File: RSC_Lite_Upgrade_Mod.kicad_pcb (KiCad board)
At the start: 2 copper layers, 36.8 x 48 mm, 30 parts, among them J1 USB_B_Micro, J2 Boot Mode, J3 SWD, J4 JTAG, SW1 RESET, U1 STM32F103C8Tx, Y1 8Mhz

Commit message: Add gerbers and firmware for revision 1
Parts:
- added R9: 1.5K, Resistor_SMD:R_1206_3216Metric_Pad1.30x1.75mm_HandSolder, F.Cu at (214.1, 54.4)
- C1: value 1uF -> 100nF
- R6: value 10K -> 1K
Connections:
- RN1 pad 1: GND -> VCC
- RN1 pad 2: GND -> VCC
- RN1 pad 3: GND -> VCC
- RN1 pad 4: GND -> VCC
- RN2 pad 1: GND -> VCC
- RN2 pad 2: GND -> VCC
- RN2 pad 3: GND -> VCC
- RN2 pad 4: GND -> VCC
- U1 pad 29: unconnected-(U1-PA8-Pad29) -> /USB_PULL
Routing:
- net VCC: track 152.1 -> 181.6 mm, vias 8 -> 10
- net /USB_PULL: track 0.00 -> 20.2 mm, vias 0 -> 2
- net /USB_D+: track 24.3 -> 29.4 mm, vias 2 -> 4
- net GND: track 348.9 -> 346.9 mm, vias 26 -> 27
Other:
- board text added: "Rev.1"
- board text removed: "Rev.0"

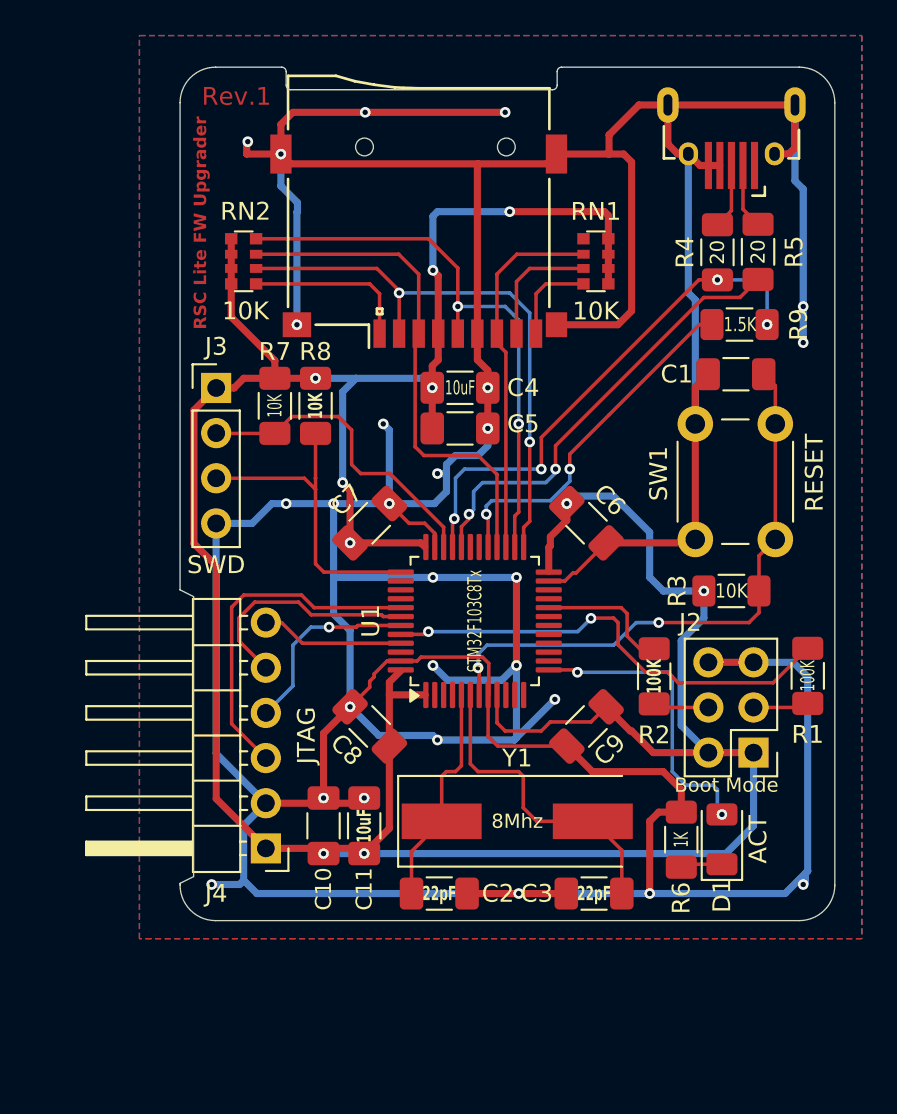
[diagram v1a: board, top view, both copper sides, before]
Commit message: Begin removing unnecessary components
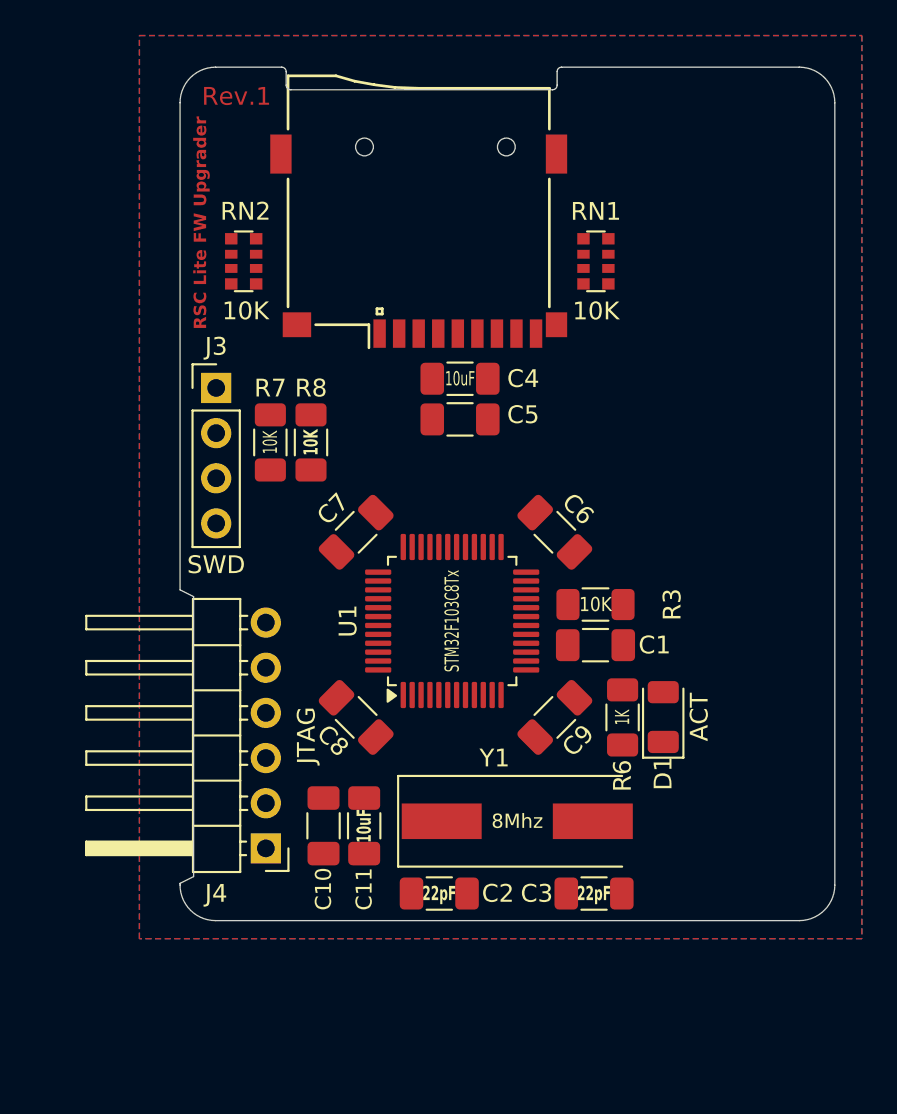
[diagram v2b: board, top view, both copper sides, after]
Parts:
- removed J1: USB_B_Micro, mod:Conn_USBmicro-B_ebay-side_TH
- removed J2: Boot Mode, Connector_PinHeader_2.54mm:PinHeader_2x03_P2.54mm_Vertical
- removed R1, R2: 100K, Resistor_SMD:R_1206_3216Metric_Pad1.30x1.75mm_HandSolder
- removed R4, R5: 20, Resistor_SMD:R_1206_3216Metric_Pad1.30x1.75mm_HandSolder
- removed R9: 1.5K, Resistor_SMD:R_1206_3216Metric_Pad1.30x1.75mm_HandSolder
- removed SW1: RESET, Button_Switch_THT:SW_PUSH_6mm
- moved C1 17.2 mm to (206.0, 72.4), turned to 0 degrees
- moved R3 7.68 mm to (206.0, 70.1), turned to 0 degrees
- moved D1 7.63 mm to (209.8, 76.4)
- moved R6 7.63 mm to (207.5, 76.5)
- moved R7 2.07 mm to (187.7, 61.0)
- moved R8 2.07 mm to (190.0, 61.0)
- moved C6 1.85 mm to (203.7, 66.0)
- moved C9 1.85 mm to (203.7, 76.5)
- moved U1 1.27 mm to (197.9, 71.0)
- moved C7 0.92 mm to (192.5, 66.0)
- moved C8 0.92 mm to (192.5, 76.5)
- moved C5 0.51 mm to (198.4, 59.7)
- moved C4 0.51 mm to (198.4, 57.4)
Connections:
- U1 pad 29: /USB_PULL -> unconnected-(U1-PA8-Pad29)
- U1 pad 44: /BOOT0 -> GND
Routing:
- net GND: track 346.9 -> 0.00 mm, vias 27 -> 0
- net VCC: track 181.6 -> 0.00 mm, vias 10 -> 0
- net /~{RESET}: track 33.2 -> 0.00 mm, vias 2 -> 0
- net /SPI2_SCK: track 32.3 -> 0.00 mm, vias 2 -> 0
- net /SPI2_SD_CS: track 32.1 -> 0.00 mm, vias 2 -> 0
- net /USB_D+: track 29.4 -> 0.00 mm, vias 4 -> 0
- net /SPI2_MOSI: track 28.7 -> 0.00 mm
- net /BOOT0: track 26.3 -> 0.00 mm, vias 2 -> 0
- net /USB_D-: track 25.2 -> 0.00 mm, vias 2 -> 0
- net /SPI2_MISO: track 20.9 -> 0.00 mm
- net /USB_PULL: track 20.2 -> 0.00 mm, vias 2 -> 0
- net /JTAG_TDO: track 19.4 -> 0.00 mm
- net /SWCLK: track 18.2 -> 0.00 mm
- net /SWDIO: track 18.0 -> 0.00 mm
- net Net-(U1-PD1): track 17.9 -> 0.00 mm
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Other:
- board text removed: "BOOT0"
- board text removed: "BOOT1"

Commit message: Rerouted the board
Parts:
- removed the C10 at (190.7, 82.5)
- C1, C2, C3, C4, C5, C6, C7, C8, C9: footprint Capacitor_SMD:C_1206_3216Metric_Pad1.33x1.80mm_HandSolder -> Capacitor_SMD:C_0805_2012Metric_Pad1.18x1.45mm_HandSolder
- C10: renamed from C11; footprint Capacitor_SMD:C_1206_3216Metric_Pad1.33x1.80mm_HandSolder -> Capacitor_SMD:C_0805_2012Metric_Pad1.18x1.45mm_HandSolder
- D1: footprint LED_SMD:LED_1206_3216Metric -> LED_SMD:LED_0805_2012Metric_Pad1.15x1.40mm_HandSolder
- R3, R6, R7, R8: footprint Resistor_SMD:R_1206_3216Metric_Pad1.30x1.75mm_HandSolder -> Resistor_SMD:R_0805_2012Metric_Pad1.20x1.40mm_HandSolder
- moved C3 12.0 mm to (196.6, 78.7)
- moved C2 9.22 mm to (192.0, 78.7)
- moved D1 6.63 mm to (203.2, 77.0)
- moved Y1 6.27 mm to (195.3, 82.5)
- moved R6 6.12 mm to (203.2, 80.8), turned to -90 degrees
- moved C10 5.67 mm to (187.5, 83.8)
- moved RN1 3.88 mm to (202.9, 53.1)
- moved C1 3.81 mm to (202.2, 72.4)
- moved C6 3.81 mm to (199.9, 66.0)
- moved C7 3.81 mm to (188.7, 66.0)
- moved C8 3.81 mm to (188.7, 76.5)
- moved C9 3.81 mm to (199.9, 76.5)
- moved R3 3.81 mm to (202.2, 70.1)
- moved U1 3.81 mm to (194.1, 71.0)
- moved XS1 3.39 mm to (193.5, 46.7)
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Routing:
- net GND: track 0.00 -> 237.2 mm, vias 0 -> 26
- net VCC: track 0.00 -> 172.3 mm, vias 0 -> 6
- net /SPI2_SCK: track 0.00 -> 31.4 mm, vias 0 -> 3
- net /SPI2_MOSI: track 0.00 -> 27.8 mm, vias 0 -> 2
- net /SPI2_MISO: track 0.00 -> 24.9 mm
- net /SPI2_SD_CS: track 0.00 -> 23.9 mm
- net /JTAG_TDO: track 0.00 -> 15.6 mm, vias 0 -> 1
- net /SWCLK: track 0.00 -> 13.4 mm
- net /SWDIO: track 0.00 -> 13.4 mm
- net Net-(U1-PD1): track 0.00 -> 11.6 mm
- net /~{RESET}: track 0.00 -> 11.4 mm, vias 0 -> 2
- net /JTAG_TCK: track 0.00 -> 9.87 mm, vias 0 -> 1
- net Net-(U1-PD0): track 0.00 -> 9.13 mm
- net Net-(RN2-R4.2): track 0.00 -> 9.03 mm
- net /JTAG_TDI: track 0.00 -> 7.91 mm, vias 0 -> 1
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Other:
- board size 36.8 x 48 mm -> 21.8 x 42.4 mm
- board text removed: "RSC Lite FW Upgrader"
- board text removed: "Rev.1"

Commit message: Route again
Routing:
- net GND: track 237.2 -> 242.0 mm, vias 26 -> 28
- net VCC: track 172.3 -> 172.9 mm
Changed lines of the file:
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@@
 		)
 		(property "Value" "JTAG"
-			(at -2.54 10.414 90)
+			(at -1.778 10.414 90)
 			(layer "F.SilkS")
 			(effects
@@
 		)
 		(property "Value" "SWD"
-			(at 2.54 9.144 90)
+			(at 0.254 9.906 180)
 			(layer "F.SilkS")
 			(effects
@@
 	)
 	(gr_text "GND"
-		(at 185.928 65.532 0)
+		(at 185.928 67.31 0)
 		(layer "B.SilkS")
 		(effects
@@
 	)
 	(gr_text "TDO"
-		(at 188.722 78.74 0)
+		(at 185.674 78.74 0)
 		(layer "B.SilkS")
 		(effects
@@
 	)
 	(gr_text "SWDIO"
-		(at 185.674 64.278 0)
+		(at 185.674 62.23 0)
 		(layer "B.SilkS")
 		(effects
@@
 	)
 	(gr_text "VCC"
-		(at 185.674 61.738 0)
+		(at 185.674 59.69 0)
 		(layer "B.SilkS")
 		(effects
@@
 	)
 	(gr_text "TMS"
-		(at 188.722 71.12 0)
+		(at 185.674 71.12 0)
 		(layer "B.SilkS")
 		(effects
@@
 	)
 	(gr_text "TDI"
-		(at 188.722 73.66 0)
+		(at 185.674 73.66 0)
 		(layer "B.SilkS")
 		(effects
@@
 	)
 	(gr_text "TCK"
-		(at 188.722 76.2 0)
+		(at 185.674 76.2 0)
 		(layer "B.SilkS")
 		(effects
@@
 	)
 	(gr_text "VCC"
-		(at 188.722 83.82 0)
+		(at 185.674 83.82 0)
 		(layer "B.SilkS")
 		(effects
@@
 	)
 	(gr_text "GND"
-		(at 188.722 81.28 0)
+		(at 185.674 81.28 0)
 		(layer "B.SilkS")
 		(effects
@@
 	)
 	(segment
+		(start 186.182 74.676)
+		(end 186.944 74.676)
+		(width 0.2)
+		(layer "F.Cu")
+		(net 2)
+	)
+	(segment
 		(start 190.997646 72.644)
 		(end 190.997646 72.048736)
@@
 	)
 	(segment
+		(start 186.944 74.676)
+		(end 187.988377 75.720377)
+		(width 0.2)
+		(layer "F.Cu")
+		(net 2)
+	)
+	(segment
 		(start 187.988377 74.139623)
 		(end 188.846854 73.281146)
@@
 	)
 	(segment
+		(start 185.928 68.58)
+		(end 184.658 67.31)
+		(width 0.2)
+		(layer "F.Cu")
+		(net 2)
+	)
+	(segment
 		(start 199.136 78.232)
 		(end 199.898 78.994)
@@
 	)
 	(segment
+		(start 185.928 69.342)
+		(end 185.928 68.58)
+		(width 0.2)
+		(layer "F.Cu")
+		(net 2)
+	)
+	(segment
 		(start 194.564 72.644)
 		(end 191.77 72.644)
@@
 	)
 	(via
+		(at 185.928 69.342)
+		(size 0.6)
+		(drill 0.3)
+		(layers "F.Cu" "B.Cu")
+		(free yes)
+		(net 2)
+	)
+	(via
 		(at 194.31 78.74)
 		(size 0.6)
@@
 	)
 	(via
+		(at 186.182 74.676)
+		(size 0.6)
+		(drill 0.3)
+		(layers "F.Cu" "B.Cu")
+		(free yes)
+		(net 2)
+	)
+	(via
 		(at 194.31 71.374)
 		(size 0.6)
@@
 	)
 	(segment
-		(start 200.631623 75.720377)
-		(end 200.631623 84.102377)
+		(start 183.408 69.576)
+		(end 184.144884 68.839116)
 		(width 0.4)
 		(layer "B.Cu")
@@
 	)
 	(segment
-		(start 186.182 65.786)
-		(end 186.182 67.828233)
+		(start 184.658 83.82)
+		(end 183.408 82.57)
+		(width 0.4)
+		(layer "B.Cu")
+		(net 5)
+	)
+	(segment
+		(start 200.631623 75.720377)
+		(end 200.631623 84.102377)
 		(width 0.4)
 		(layer "B.Cu")
@@
 	)
 	(segment
-		(start 183.408 70.602233)
-		(end 183.408 82.57)
+		(start 185.171116 68.839116)
+		(end 186.182 67.828233)
 		(width 0.4)
 		(layer "B.Cu")
@@
 	(segment
 		(start 183.408 82.57)
-		(end 184.658 83.82)
+		(end 183.408 69.576)
 		(width 0.4)
 		(layer "B.Cu")
@@
 	(segment
 		(start 186.182 67.828233)
-		(end 183.408 70.602233)
+		(end 186.182 65.786)
 		(width 0.4)
 		(layer "B.Cu")
@@
 		(width 0.4)
 		(layer "B.Cu")
+		(net 5)
+	)
+	(segment
+		(start 184.144884 68.839116)
+		(end 185.171116 68.839116)
+		(width 0.4)
+		(layer "B.Cu")

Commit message: Some more rerouting
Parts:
- U1: value STM32F103C8Tx -> 32F103C8T6
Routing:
- net GND: track 242.0 -> 247.7 mm, vias 28 -> 30
- net /SPI2_MISO: track 24.9 -> 19.6 mm
- net /SPI2_MOSI: track 27.8 -> 23.6 mm, vias 2 -> 0
- net /SPI2_SD_CS: track 23.9 -> 28.0 mm, vias 0 -> 2
- net VCC: track 172.9 -> 174.7 mm
- net /SPI2_SCK: track 31.4 -> 32.2 mm

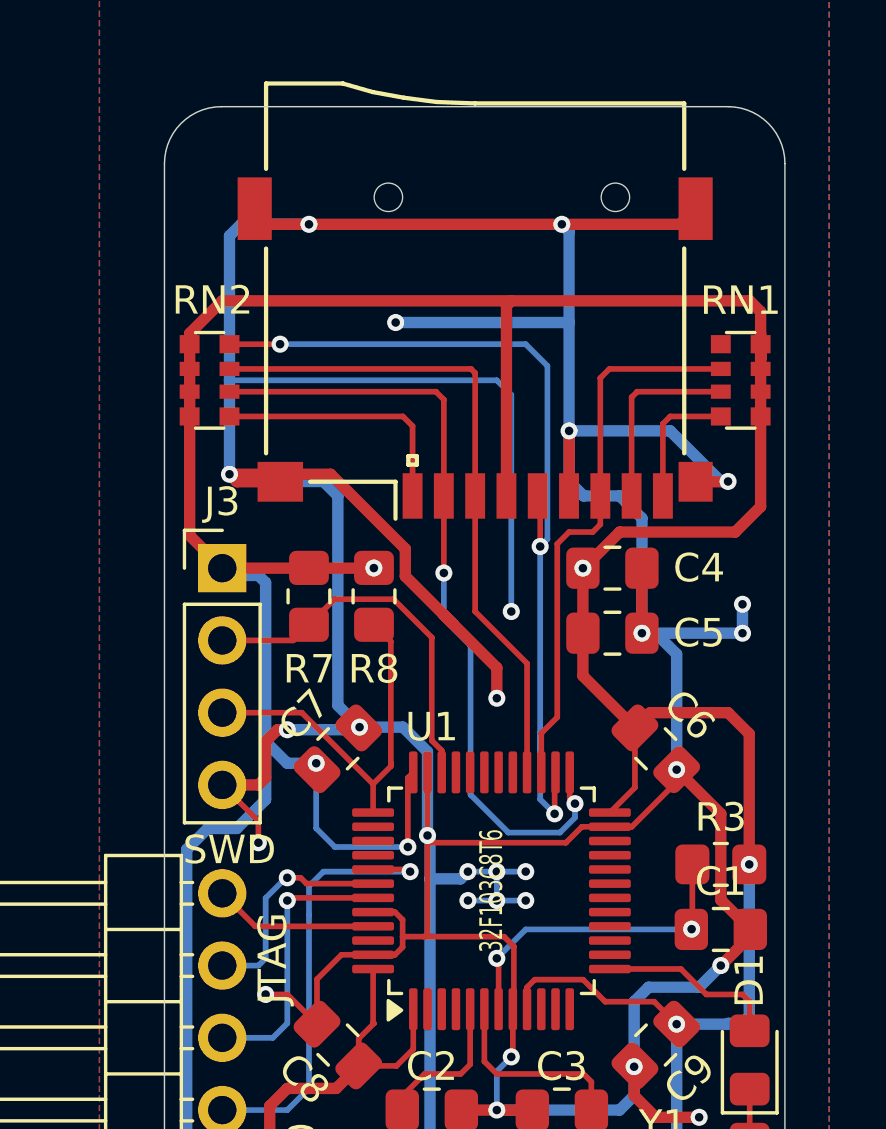
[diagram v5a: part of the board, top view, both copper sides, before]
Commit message: Update some routing and silkscreen
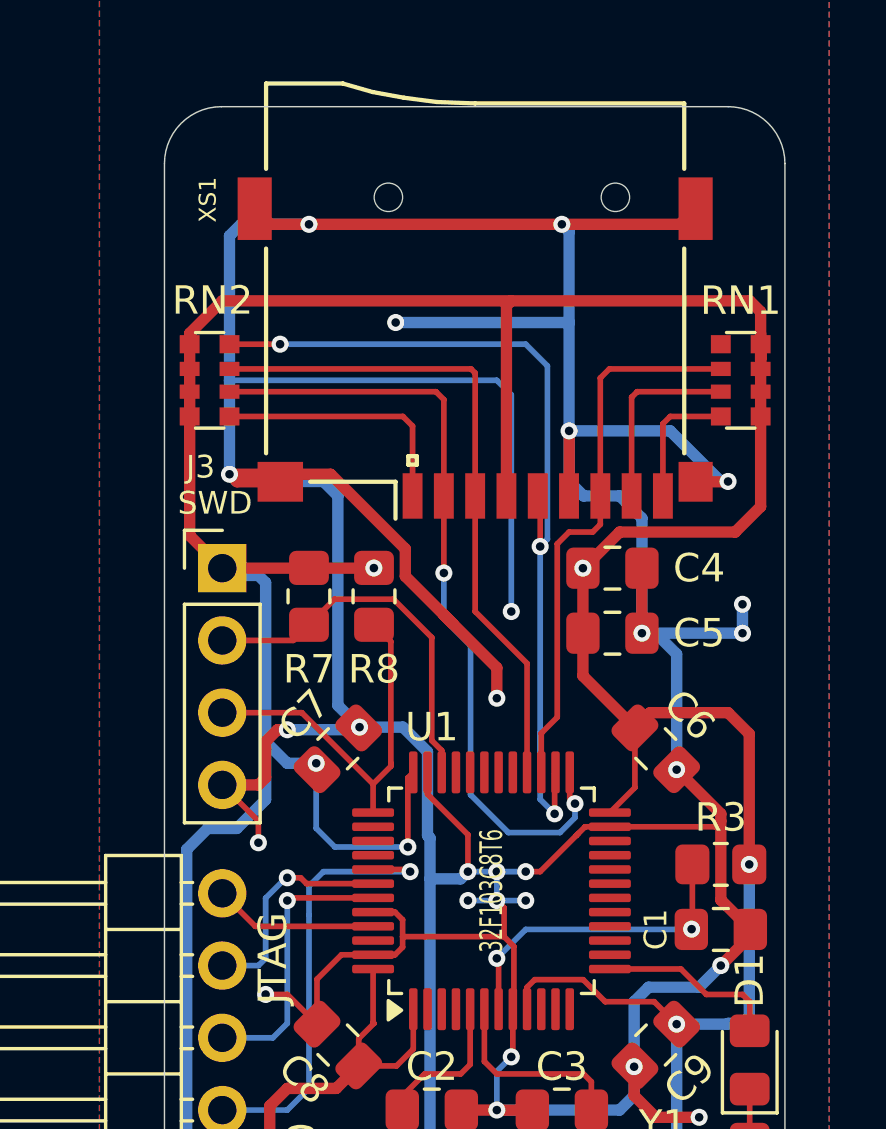
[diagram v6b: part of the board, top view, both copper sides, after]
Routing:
- net GND: track 247.7 -> 245.4 mm, vias 30 -> 29
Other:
- board text added: "Lava RSC Lite Upgrade board"
- board text added: "Rev.2"
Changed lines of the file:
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@@
 		(at 193.548 46.652 180)
 		(property "Reference" "XS1"
-			(at 0 1 0)
-			(layer "F.Fab")
+			(at 9.398 -0.084 90)
+			(layer "F.SilkS")
 			(effects
 				(font
@@
 		(tags "Through hole pin header THT 1x04 2.54mm single row")
 		(property "Reference" "J3"
-			(at 0 -2.33 0)
+			(at -0.762 -3.556 0)
 			(layer "F.SilkS")
 			(effects
 				(font
-					(size 1 1)
+					(size 0.8 0.8)
 					(thickness 0.15)
 				)
@@
 		)
 		(property "Value" "SWD"
-			(at 0.254 9.906 180)
+			(at -0.254 -2.286 180)
 			(layer "F.SilkS")
 			(effects
 				(font
-					(size 1 1)
+					(size 0.8 0.8)
 					(thickness 0.15)
 				)
@@
 		(tags "capacitor handsolder")
 		(property "Reference" "C1"
-			(at 0 -1.68 0)
+			(at -2.286 0 90)
 			(layer "F.SilkS")
 			(effects
 				(font
-					(size 1 1)
+					(size 0.8 0.8)
 					(thickness 0.15)
 				)
@@
 		)
 	)
+	(gr_text "Lava RSC Lite Upgrade board"
+		(at 201.93 60.706 90)
+		(layer "B.SilkS")
+		(effects
+			(font
+				(size 2 1.4)
+				(thickness 0.3)
+				(bold yes)
+			)
+			(justify mirror)
+		)
+	)
 	(gr_text "SWDIO"
 		(at 185.674 62.23 0)
@@
 		)
 	)
+	(gr_text "Rev.2"
+		(at 202.438 82.804 90)
+		(layer "B.SilkS")
+		(effects
+			(font
+				(size 1 0.7)
+				(thickness 0.15)
+				(bold yes)
+			)
+			(justify mirror)
+		)
+	)
 	(gr_text "TMS"
 		(at 185.674 71.12 0)
@@
 	)
 	(segment
-		(start 199.055056 68.781146)
-		(end 200.631623 67.204579)
-		(width 0.2)
-		(layer "F.Cu")
-		(net 2)
-	)
-	(segment
 		(start 186.182 74.676)
 		(end 186.944 74.676)
@@
 	)
 	(segment
-		(start 202.428 56.652)
-		(end 202.438 56.642)
-		(width 0.4)
+		(start 198.285146 68.781146)
+		(end 201.982854 68.781146)
+		(width 0.2)
 		(layer "F.Cu")
 		(net 2)
 	)
 	(segment
-		(start 194.31 63.191106)
-		(end 194.31 64.262)
+		(start 202.428 56.652)
+		(end 202.438 56.642)
 		(width 0.4)
 		(layer "F.Cu")
@@
 	)
 	(segment
-		(start 202.184 71.3525)
-		(end 202.184 68.326)
+		(start 194.31 63.191106)
+		(end 194.31 64.262)
 		(width 0.4)
 		(layer "F.Cu")
@@
 	)
 	(segment
+		(start 194.564 71.628)
+		(end 194.31 71.374)
+		(width 0.2)
+		(layer "F.Cu")
+		(net 2)
+	)
+	(segment
 		(start 186.944 74.676)
 		(end 187.988377 75.720377)
@@
 	)
 	(segment
+		(start 197.104 69.088)
+		(end 195.834 70.358)
+		(width 0.2)
+		(layer "F.Cu")
+		(net 2)
+	)
+	(segment
 		(start 186.182 65.786)
 		(end 186.598 65.37)
@@
 	)
 	(segment
+		(start 191.872646 67.638556)
+		(end 193.294 69.05991)
+		(width 0.2)
+		(layer "F.Cu")
+		(net 2)
+	)
+	(segment
 		(start 202.184 68.326)
 		(end 200.631623 66.773623)
@@
 	)
 	(segment
-		(start 199.136 78.232)
-		(end 199.898 78.994)
-		(width 0.4)
+		(start 195.834 70.358)
+		(end 195.326 70.358)
+		(width 0.2)
 		(layer "F.Cu")
 		(net 2)
 	)
 	(segment
-		(start 198.285146 68.781146)
-		(end 197.301069 68.781146)
-		(width 0.2)
+		(start 199.136 78.232)
+		(end 199.898 78.994)
+		(width 0.4)
 		(layer "F.Cu")
 		(net 2)
@@
 	)
 	(segment
+		(start 193.294 69.05991)
+		(end 193.294 70.358)
+		(width 0.2)
+		(layer "F.Cu")
+		(net 2)
+	)
+	(segment
 		(start 189.455623 65.306377)
 		(end 189.484 65.278)
@@
 	)
 	(segment
-		(start 191.872646 66.868646)
-		(end 191.872646 69.088)
-		(width 0.2)
-		(layer "F.Cu")
-		(net 2)
-	)
-	(segment
 		(start 190.730056 71.781146)
 		(end 189.960146 71.781146)
@@
 	)
 	(segment
-		(start 196.740215 69.342)
-		(end 191.872646 69.342)
-		(width 0.2)
-		(layer "F.Cu")
-		(net 2)
-	)
-	(segment
 		(start 203.2215 72.39)
 		(end 202.184 71.3525)
@@
 	)
 	(segment
-		(start 198.285146 68.781146)
-		(end 199.055056 68.781146)
-		(width 0.2)
-		(layer "F.Cu")
-		(net 2)
-	)
-	(segment
 		(start 194.872646 75.193646)
 		(end 194.872646 76.815354)
@@
 	)
 	(segment
+		(start 201.982854 68.781146)
+		(end 202.184 68.58)
+		(width 0.2)
+		(layer "F.Cu")
+		(net 2)
+	)
+	(segment
+		(start 197.410854 68.781146)
+		(end 198.285146 68.781146)
+		(width 0.2)
+		(layer "F.Cu")
+		(net 2)
+	)
+	(segment
 		(start 196.596 47.602)
 		(end 187.706 47.602)
@@
 	)
 	(segment
-		(start 191.872646 69.088)
-		(end 191.872646 69.342)
-		(width 0.2)
+		(start 202.184 71.3525)
+		(end 202.184 68.58)
+		(width 0.4)
 		(layer "F.Cu")
 		(net 2)
@@
 	)
 	(segment
-		(start 191.872646 72.541354)
-		(end 191.77 72.644)
-		(width 0.2)
-		(layer "F.Cu")
-		(net 2)
-	)
-	(segment
 		(start 192.786 61.667106)
 		(end 192.432447 61.313553)
@@
 	)
 	(segment
+		(start 197.104 69.088)
+		(end 197.410854 68.781146)
+		(width 0.2)
+		(layer "F.Cu")
+		(net 2)
+	)
+	(segment
 		(start 194.91 75.156292)
 		(end 194.91 72.99)
@@
 	)
 	(segment
-		(start 197.301069 68.781146)
-		(end 196.740215 69.342)
-		(width 0.2)
-		(layer "F.Cu")
-		(net 2)
-	)
-	(segment
 		(start 193.0615 78.74)
 		(end 194.31 78.74)
@@
 	)
 	(segment
-		(start 191.872646 69.342)
-		(end 191.872646 72.541354)
+		(start 190.730056 73.281146)
+		(end 190.997646 73.013556)
 		(width 0.2)
 		(layer "F.Cu")
@@
 	)
 	(segment
-		(start 190.730056 73.281146)
-		(end 190.997646 73.013556)
+		(start 194.564 72.644)
+		(end 194.564 71.628)
 		(width 0.2)
 		(layer "F.Cu")
@@
 	)
 	(segment
+		(start 202.184 68.58)
+		(end 202.184 68.326)
+		(width 0.4)
+		(layer "F.Cu")
+		(net 2)
+	)
+	(segment
 		(start 186.182 66.04)
 		(end 186.182 65.786)
@@
 	)
 	(segment
+		(start 191.872646 66.868646)
+		(end 191.872646 67.638556)
+		(width 0.2)
+		(layer "F.Cu")
+		(net 2)
+	)
+	(segment
 		(start 195.5585 82.296)
 		(end 195.5585 84.222334)
@@
 	)
 	(segment
+		(start 197.176108 69.015892)
+		(end 197.104 69.088)
+		(width 0.2)
+		(layer "F.Cu")
+		(net 2)
+	)
+	(segment
 		(start 188.913334 84.243834)
 		(end 187.452 82.7825)
@@
 		(size 0.6)
 		(drill 0.3)
-		(layers "F.Cu" "B.Cu")
-		(net 2)
-	)
-	(via
-		(at 191.872646 69.088)
-		(size 0.6)
-		(drill 0.3)
